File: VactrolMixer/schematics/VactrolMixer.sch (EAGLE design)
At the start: 76 parts, among them IC1 NE5532N, IC2 NE5532N, IC6 NE5532N, T1 2N3904, T2 2N3904, T3 2N3904, T4 2N3904

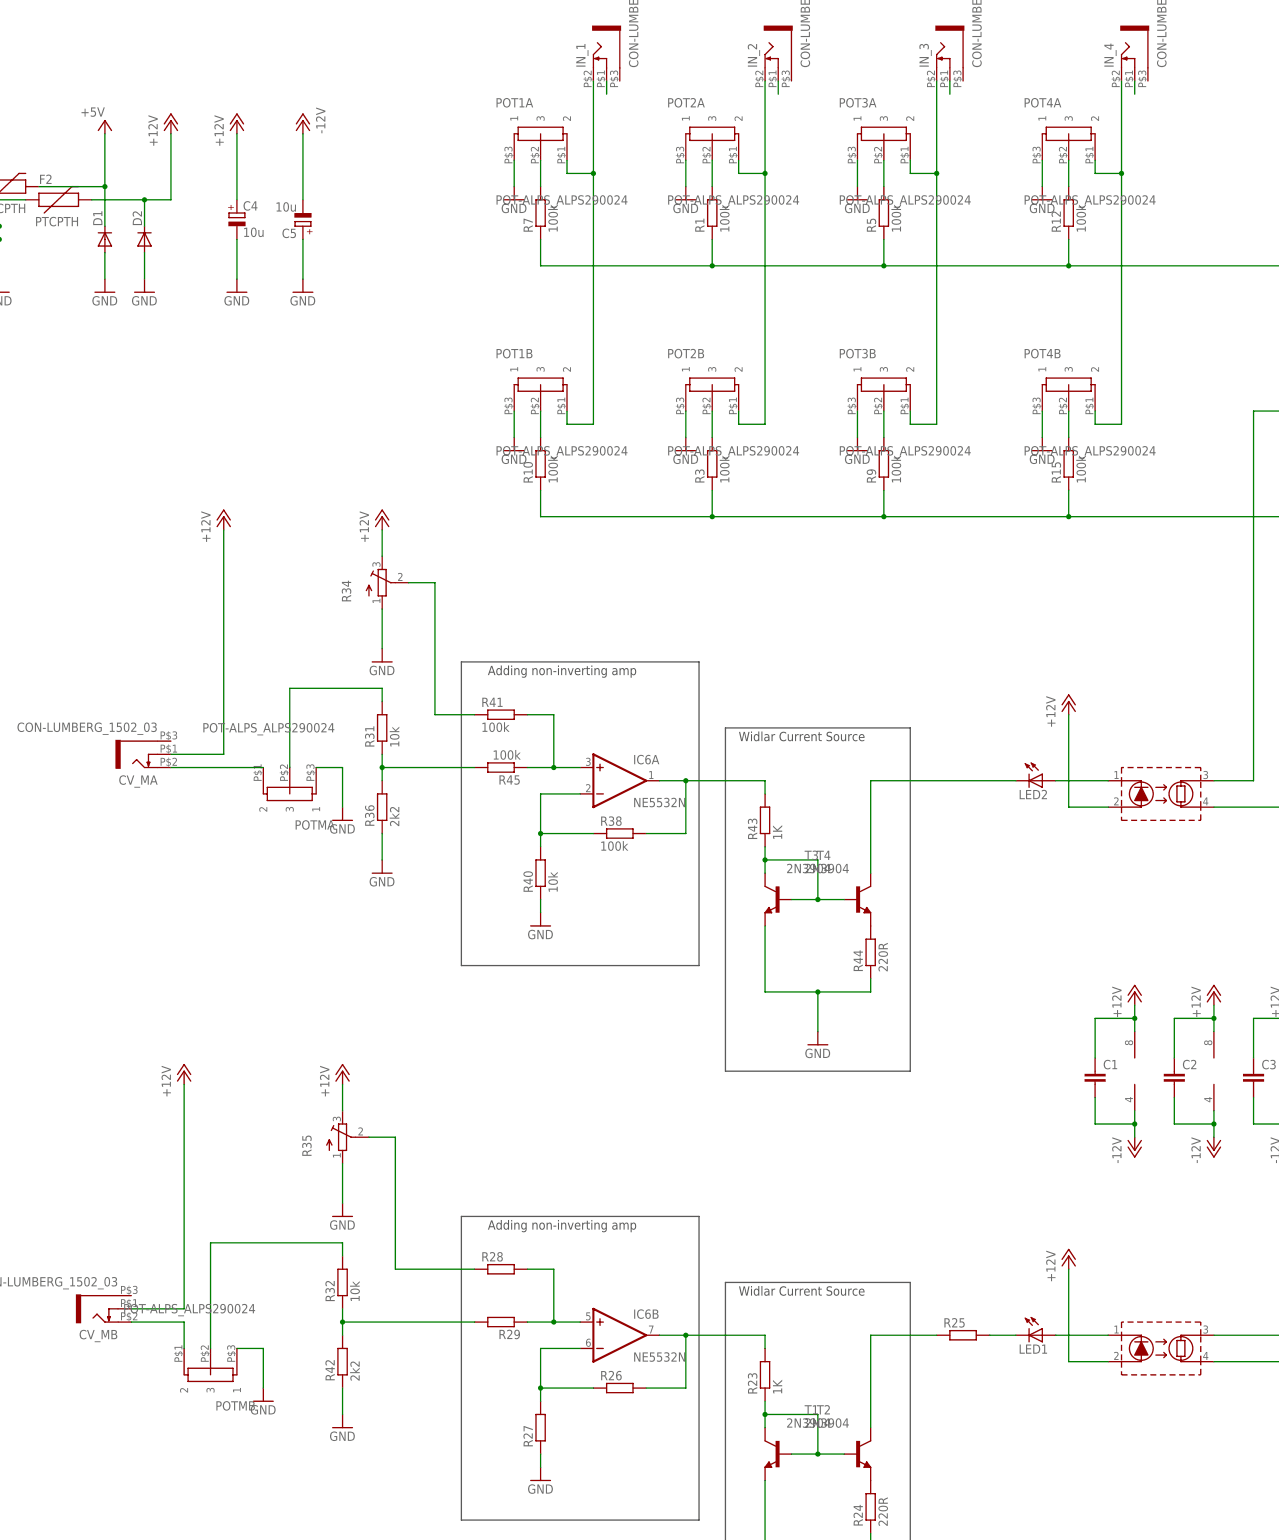
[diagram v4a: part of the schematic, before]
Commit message: changed pots
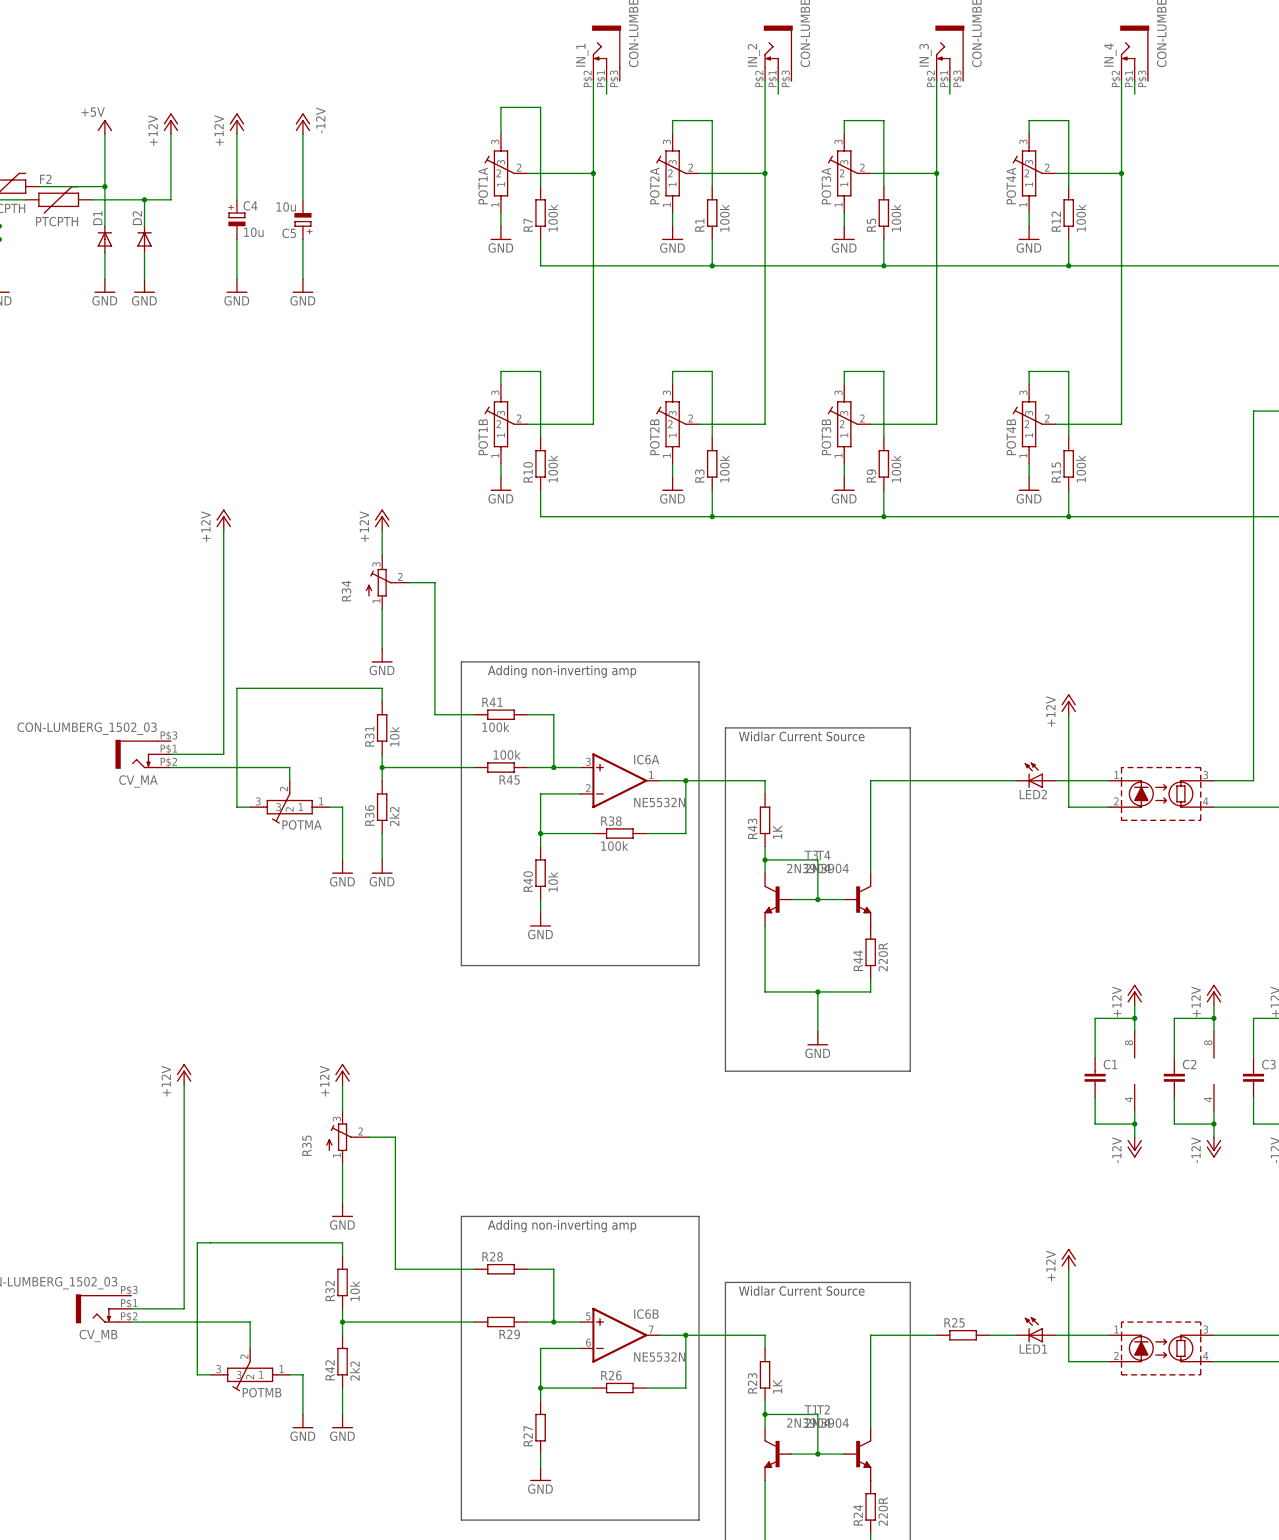
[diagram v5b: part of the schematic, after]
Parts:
- POT1A, POT1B, POT2A, POT2B, POT3A, POT3B, POT4A, POT4B, POTMA, POTMB: value POT-ALPS_ALPS290024 -> POT-ALPS-RK09L1140; device Rebel:POT-ALPS_ALPS290024 -> Rebel:POT-ALPS-RK09L1140
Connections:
- net GND: now also POT1AG$1.1, POT1BG$1.1, POT2AG$1.1, POT2BG$1.1, POT3AG$1.1, POT3BG$1.1, POT4AG$1.1, POT4BG$1.1, POTMAG$1.1, POTMBG$1.1; no longer POT1A.1, POT1B.1, POT2A.1, POT2B.1, POT3A.1, POT3B.1, POT4A.1, POT4B.1, POTMA.1, POTMB.1
- net N$12: now also POT2AG$1.3; no longer POT2A.3
- net N$13: now also POT2BG$1.3; no longer POT2B.3
- net N$18: now also POTMAG$1.3; no longer POTMA.3
- net N$19: now also POT3AG$1.2, POT3BG$1.2; no longer POT3A.2, POT3B.2
- net N$2: now also POT2AG$1.2, POT2BG$1.2; no longer POT2A.2, POT2B.2
- net N$21: now also POT3AG$1.3; no longer POT3A.3
- net N$22: now also POT3BG$1.3; no longer POT3B.3
- net N$25: now also POT4AG$1.2, POT4BG$1.2; no longer POT4A.2, POT4B.2
- net N$33: now also POT1AG$1.2, POT1BG$1.2; no longer POT1A.2, POT1B.2
- net N$37: now also POTMBG$1.3; no longer POTMB.3
- net N$38: now also POTMBG$1.2; no longer POTMB.2
- net N$43: now also POT1AG$1.3; no longer POT1A.3
- net N$45: now also POT4AG$1.3; no longer POT4A.3
- net N$46: now also POT4BG$1.3; no longer POT4B.3
- net N$47: now also POT1BG$1.3; no longer POT1B.3
- net N$7: now also POTMAG$1.2; no longer POTMA.2

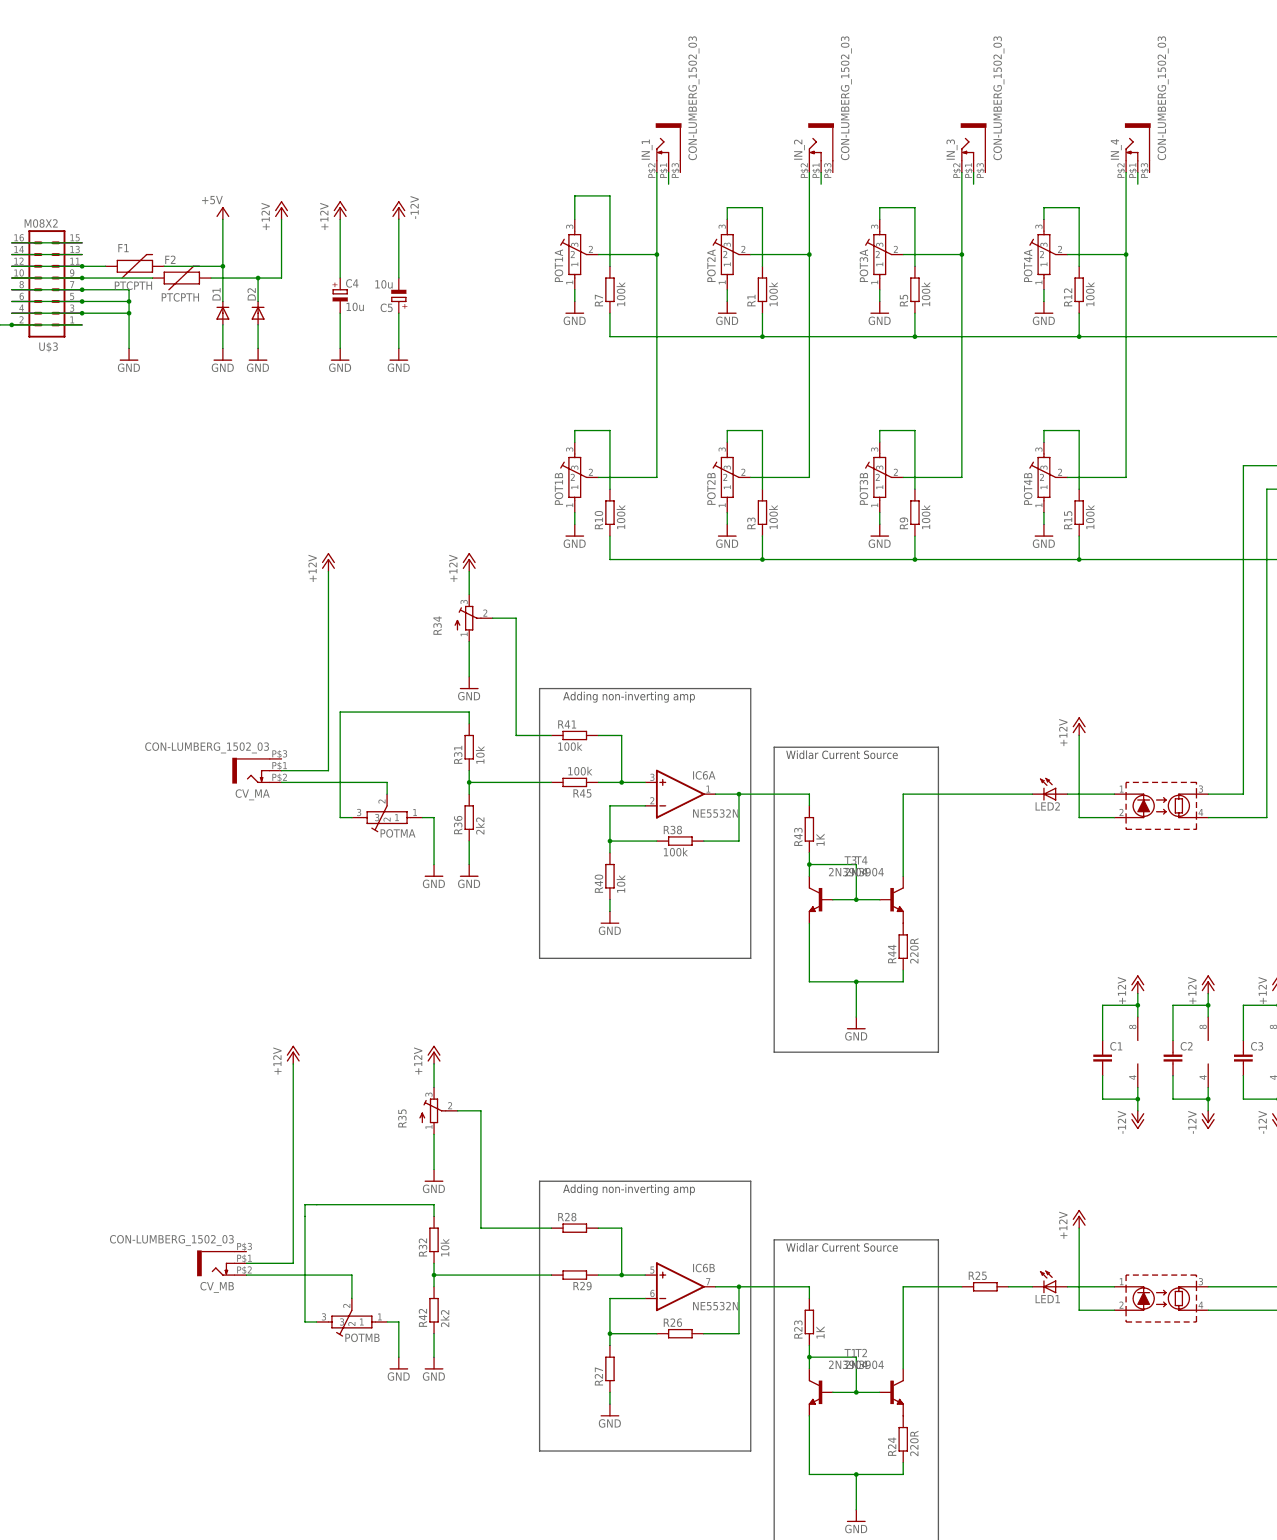
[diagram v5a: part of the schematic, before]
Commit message: updated to ensure sensible input t impedances
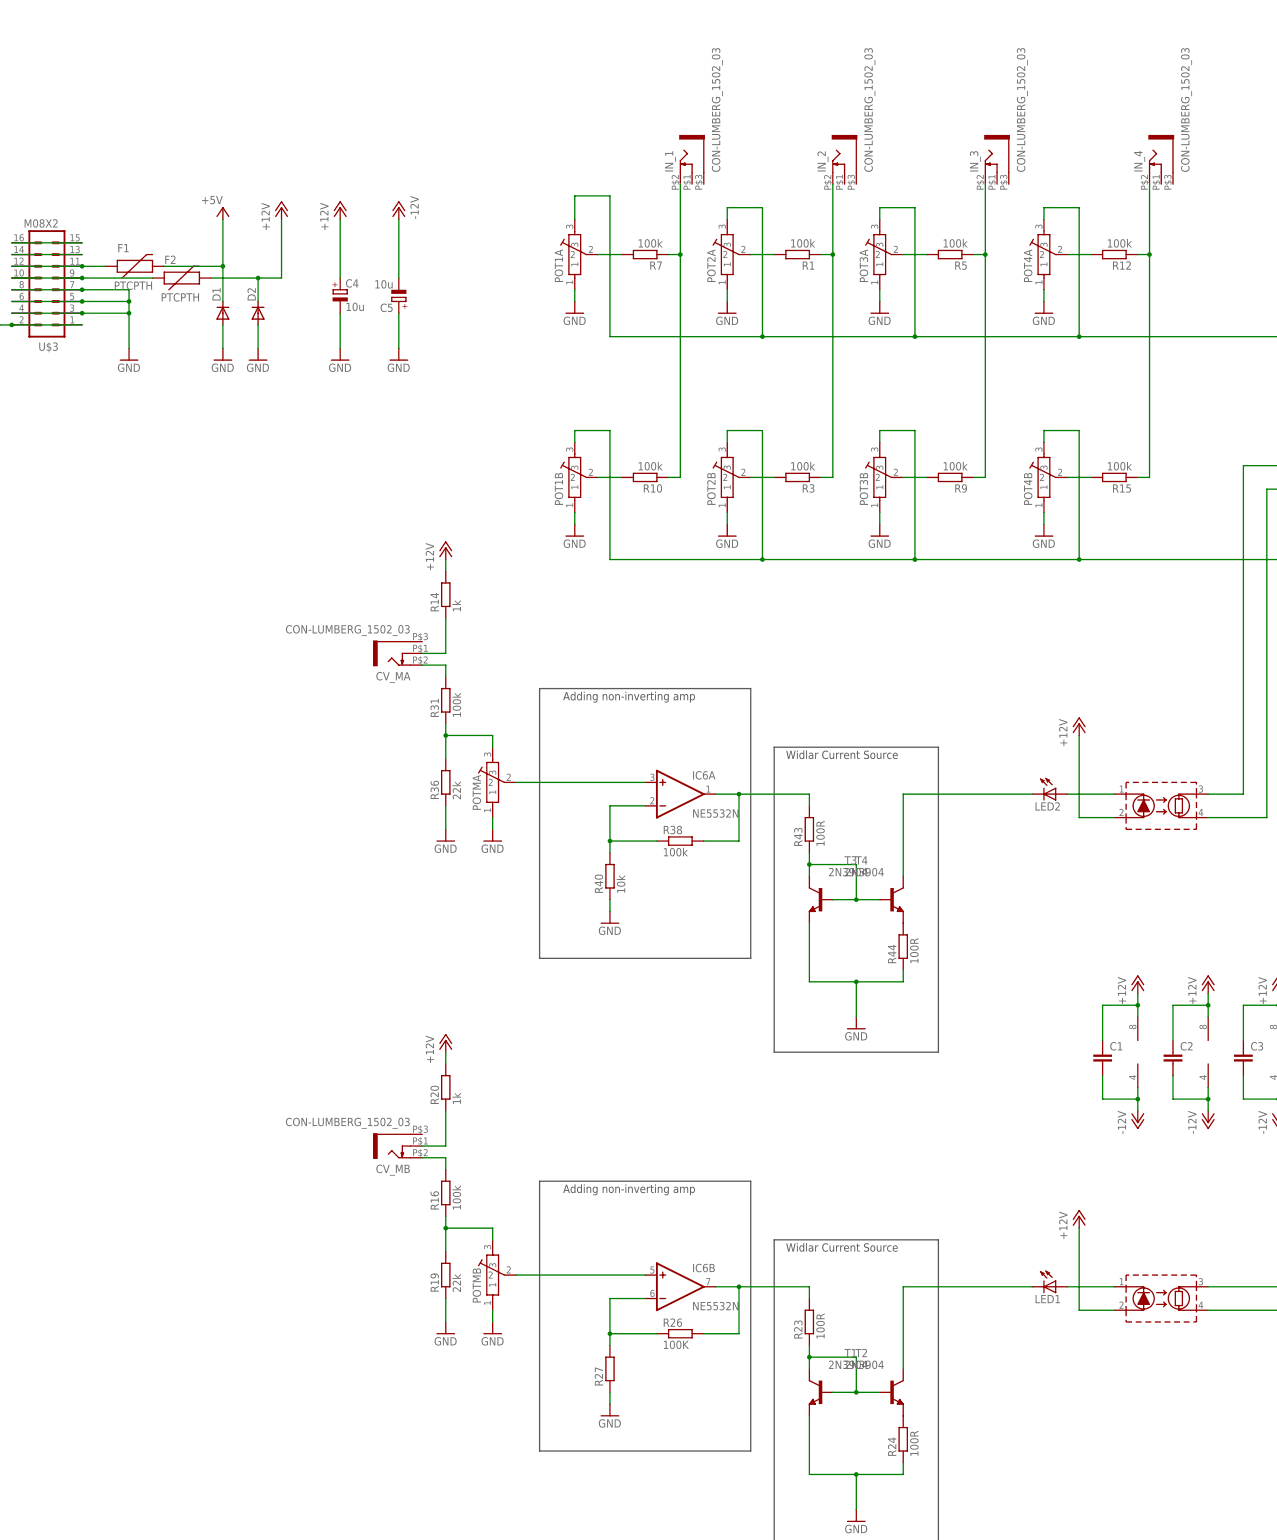
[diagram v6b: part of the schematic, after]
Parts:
- removed R25, R28, R29: (no value), resistor:R-EU_0411/15
- removed R32: 10k, resistor:R-EU_0411/15
- removed R34, R35: (no value), pot:TRIM_EU-3223W
- removed R41, R45: 100k, resistor:R-EU_0411/15
- removed R42: 2k2, resistor:R-EU_0411/15
- added R14, R20: 1k, resistor:R-EU_0411/15
- added R16: 100k, resistor:R-EU_0411/15
- added R19: 22k, resistor:R-EU_0411/15
- R23, R43: value 1K -> 100R
- R24, R44: value 220R -> 100R
- R26: value (none) -> 100K
- R31: value 10k -> 100k
- R36: value 2k2 -> 22k
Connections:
- removed net IN_C: IN_3.4
- removed net N$12: POT2AG$1.3, R1.2
- removed net N$21: POT3AG$1.3, R5.2
- removed net N$22: POT3BG$1.3, R9.2
- removed net N$23: R29.2, R32.1, R42.2
- removed net N$24: IC1A.-IN, R1.1, R12.1, R5.1, R6.1, R7.1
- removed net N$26: IC2A.-IN, R10.1, R11.1, R15.1, R3.1, R9.1
- removed net N$43: POT1AG$1.3, R7.2
- removed net N$47: POT1BG$1.3, R10.2
- new net N$49: CV_MB.3, R16.2
- new net N$52: IN_4.3, R12.1, R15.1
- net +12V: now also R14.2, R20.2; no longer CV_MA.4, CV_MB.4, R34.E, R35.E
- net GND: now also R19.1; no longer R34.A, R35.A, R42.1
- net N$10: now also POT3BG$1.2, R9.2; no longer IN_2.4
- net N$13: now also POT1AG$1.2, R7.2; no longer POT2BG$1.3, R3.2
- net N$16: now also POTMBG$1.3, R16.1, R19.2; no longer LED1.C, R25.2
- net N$18: now also CV_MA.4, R14.1; no longer POTMAG$1.3, R31.2
- net N$19: now also POT4BG$1.2, R15.2; no longer IN_3.3, POT3AG$1.2, POT3BG$1.2
- net N$2: now also R3.2; no longer IN_2.3, POT2AG$1.2
- net N$20: now also POTMAG$1.3; no longer R45.2
- net N$25: now also R12.2; no longer IN_4.3, POT4BG$1.2
- net N$29: now also LED1.C; no longer R25.1
- net N$31: now also POT3AG$1.2, R5.2; no longer R28.1, R35.S
- net N$32: now also POTMBG$1.2; no longer R28.2, R29.1
- net N$33: now also R10.2; no longer IN_1.3, POT1AG$1.2
- net N$34: now also POT2AG$1.2, R1.2; no longer IN_4.4
- net N$37: now also IN_1.3, R10.1, R7.1; no longer POTMBG$1.3, R32.2
- net N$38: now also IN_2.3, R1.1, R3.1; no longer CV_MB.3, POTMBG$1.2
- net N$41: now also IN_3.3, R5.1, R9.1; no longer IN_1.4
- net N$45: now also IC1A.-IN, POT1AG$1.3, POT2AG$1.3, POT3AG$1.3, R6.1; no longer R12.2
- net N$46: now also IC2A.-IN, POT1BG$1.3, POT2BG$1.3, POT3BG$1.3, R11.1; no longer R15.2
- net N$50: now also POTMAG$1.2; no longer R41.2, R45.1
- net N$51: now also CV_MB.4, R20.1; no longer R34.S, R41.1
- net N$7: now also R31.2; no longer POTMAG$1.2
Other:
- moved on the sheet: CV_MA, CV_MB, IN_1, IN_2, IN_3, IN_4, POTMA, POTMB, R1, R10, R12, R15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
